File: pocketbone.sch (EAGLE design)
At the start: 60 parts, among them J1 USD_CONNECTOR, U1 24LC_32AT-I/OT, U2 OSD3358, U3 SN74LVC1G07_DCK_5, Y1 CM200C-32.768KAZF-UT, Y2 445C33D24M00000

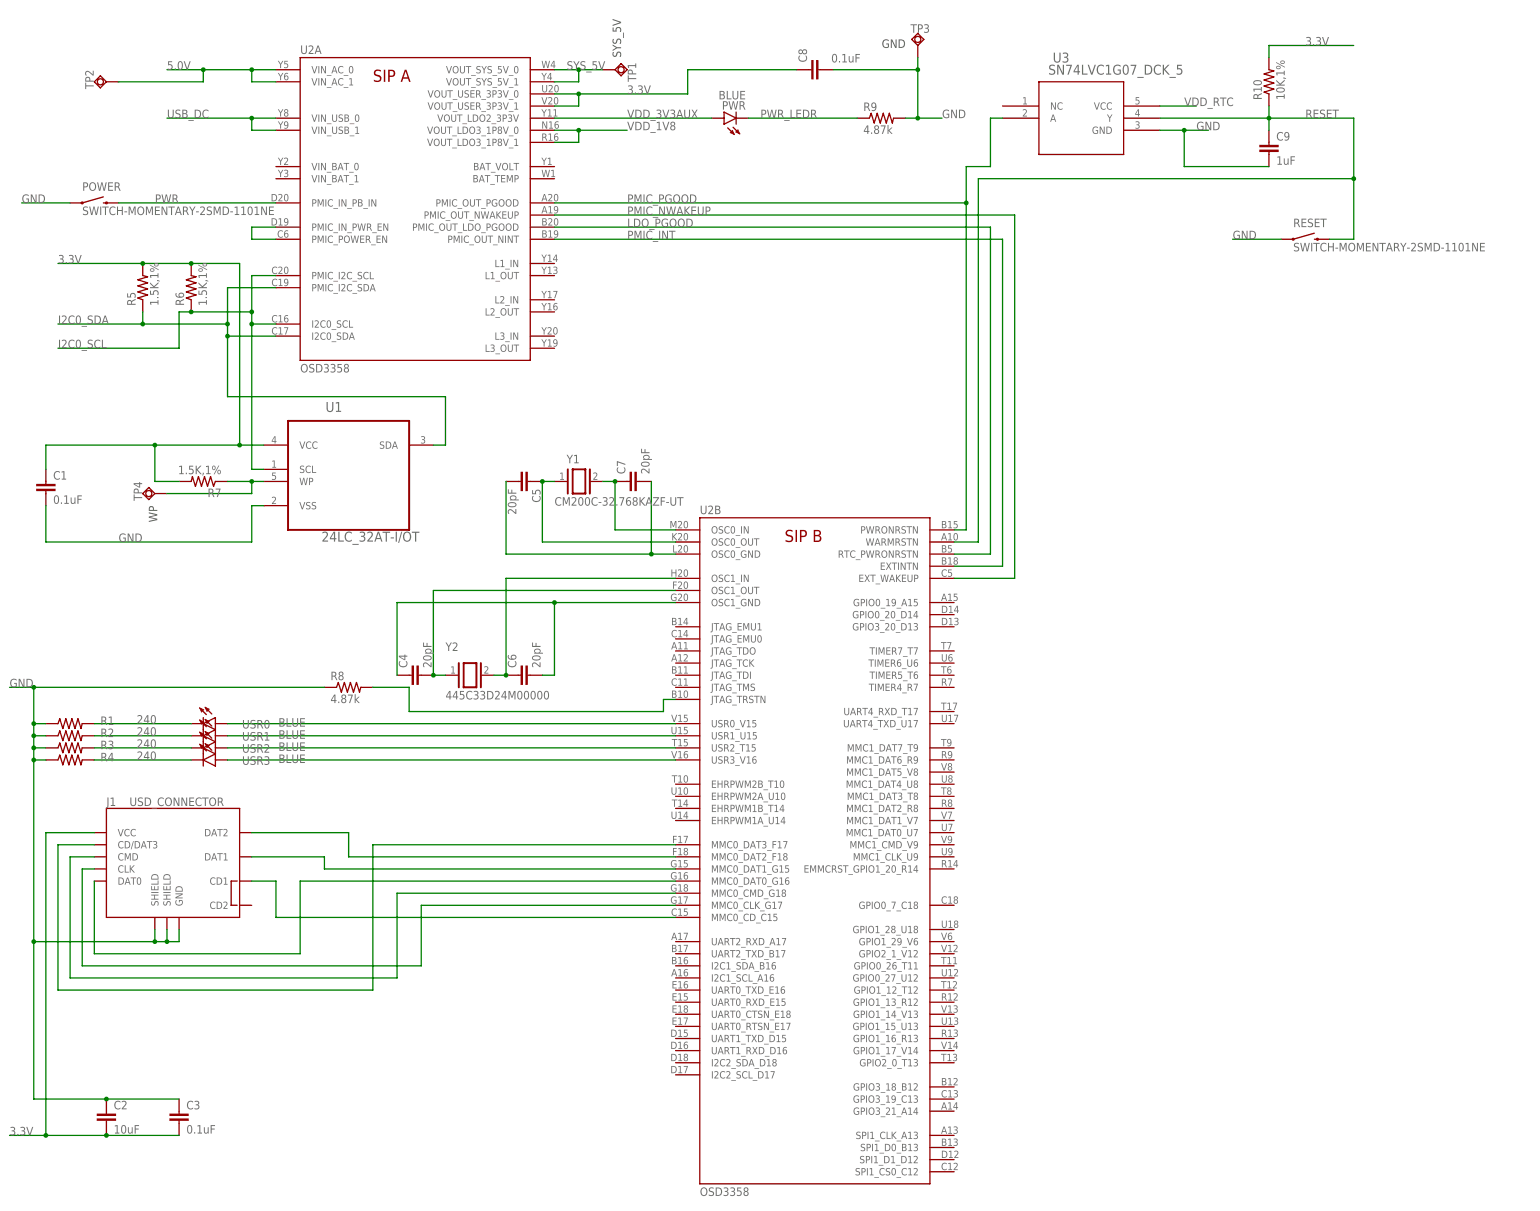
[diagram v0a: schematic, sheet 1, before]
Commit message: Reduce size (WIP) and change DRU for Seeed Studio tolerances
Signed-off-by: Andrew Yong <me@ndoo.sg>
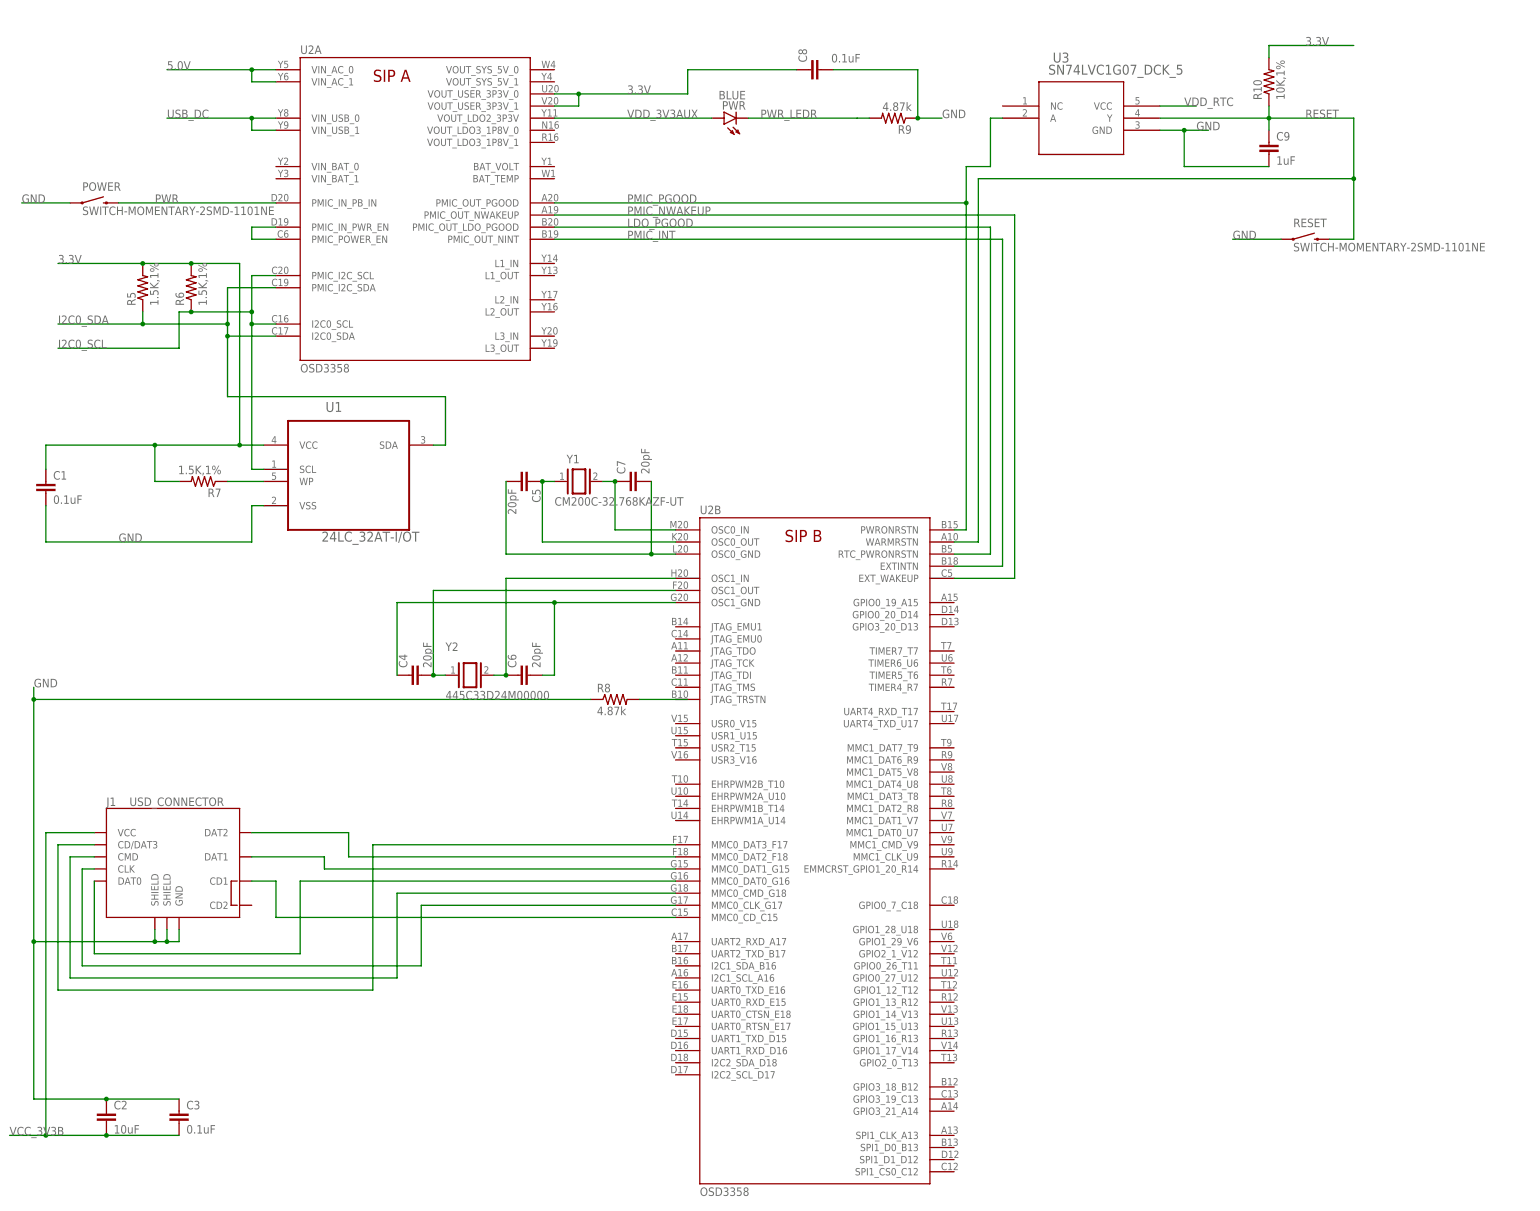
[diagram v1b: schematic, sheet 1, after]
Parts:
- removed C10: 10uF, Strawson_Eagle_Lib:CAP0805
- removed C11: 0.1uF, Strawson_Eagle_Lib:CAP0402-CAP
- removed L1: 120, Seeed-OPL-Inductor:INDUCTOR/FERRITE-BEAD'0603'
- removed R1, R2, R3, R4: 240, Strawson_Eagle_Lib:RESISTOR0402-RES
- removed R11: 0, Strawson_Eagle_Lib:RESISTOR0402-RES
- removed R12: 0,DNI, Strawson_Eagle_Lib:RESISTOR0402-RES
- removed TP1, TP2, TP3, TP4: TPSQPAD1-17, pocketbone:TPSQPAD1-17
- removed USB0, USB1: USB-MICRO-SMD, pocketbone:USB-AB
- removed USR0, USR1, USR2, USR3: BLUE, BeagleBone_Blue:LED0603
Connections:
- removed net N$1: L1.2, USB1.VBUS
- removed net N$129: C10.1, C11.1, L1.1, R11.2, R12.2, U2C.USB1_VBUS
- removed net N$43: U2B.USR3_V16, USR3.A
- removed net N$44: U2B.USR2_T15, USR2.A
- removed net N$45: U2B.USR1_U15, USR1.A
- removed net N$46: U2B.USR0_V15, USR0.A
- removed net N$47: R1.2, USR0.C
- removed net N$57: R2.2, USR1.C
- removed net N$58: R3.2, USR2.C
- removed net N$59: R4.2, USR3.C
- removed net SYS_5V: R12.1, TP1.TP, U2A.VOUT_SYS_5V_0, U2A.VOUT_SYS_5V_1
- removed net USB1_DM: U2C.USB1_DM, USB1.D-
- removed net USB1_DP: U2C.USB1_DP, USB1.D+
- removed net USB1_ID: U2C.USB1_ID, USB1.USBID
- removed net VDD_1V8: U2A.VOUT_LDO3_1P8V_0, U2A.VOUT_LDO3_1P8V_1, U2E.VDD_1V83, U2E.VDD_1V84
- new net VCC_3V3B: C2.2, C3.2, J1.VCC
- net 3.3V: no longer C2.2, C3.2, J1.VCC
- net 5.0V: no longer R11.1, TP2.TP
- net GND: now also R9.1; no longer C10.2, C11.2, R1.1, R2.1, R3.1, R4.1, R9.2, TP3.TP, USB0.GND, USB0.SHIELD, USB1.GND, USB1.SHIELD
- net N$28: no longer TP4.TP
- net PWR_LEDR: now also R9.2; no longer R9.1
- net USB0_DM: no longer USB0.D-
- net USB0_DP: no longer USB0.D+
- net USB0_ID: no longer USB0.USBID
- net USB_DC: no longer USB0.VBUS
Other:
- moved on the sheet: R8, R9
